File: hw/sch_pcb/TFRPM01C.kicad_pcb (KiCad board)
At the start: 2 copper layers, 37.5 x 19 mm, 23 parts, among them J1 HEADER_1x03, J2 SM04B-GHS-TB, J3 SM04B-GHS-TB, M2 M3, U1 PCF8583, U2 74HC1G14GW, U3 MIC5504-3.3YM5

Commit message: Edit
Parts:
- moved R1 0.44 mm to (141.5, 126.7)
- moved R2 0.44 mm to (137.2, 126.7)
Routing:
- net Net-(JP2-Pad2): track 9.91 -> 10.5 mm
- net GND: vias 61 -> 60
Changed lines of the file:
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@@
   )
   (footprint "Mlab_R:SMD-0805" (layer "B.Cu")
-    (at 141.478 126.3015 -90)
+    (at 141.478 126.746 -90)
     (property "Sheetfile" "TFRPM01C.kicad_sch")
     (property "Sheetname" "")
@@
   )
   (footprint "Mlab_R:SMD-0805" (layer "B.Cu")
-    (at 137.16 126.3015 90)
+    (at 137.16 126.746 90)
     (property "Sheetfile" "TFRPM01C.kicad_sch")
     (property "Sheetname" "")
@@
     (property "Sheetname" "")
     (attr exclude_from_pos_files)
-    (fp_text reference "JP2" (at 0 2.032) (layer "B.SilkS")
+    (fp_text reference "JP2" (at 1.016 -2.286) (layer "B.SilkS")
       (effects (font (size 1.3 1.3) (thickness 0.3)) (justify mirror))
     )
@@
   (via (at 138.176 136.903096) (size 0.8) (drill 0.4) (layers "F.Cu" "B.Cu") (net 1))
   (via (at 139.192 128.016) (size 0.8) (drill 0.4) (layers "F.Cu" "B.Cu") (net 1))
-  (via (at 136.906 128.524) (size 0.8) (drill 0.4) (layers "F.Cu" "B.Cu") (net 1))
   (via (at 143.002 135.382) (size 0.8) (drill 0.4) (layers "F.Cu" "B.Cu") (net 1))
   (via (at 143.764 138.684) (size 0.8) (drill 0.4) (layers "F.Cu" "B.Cu") (net 1))
@@
   (segment (start 129.032 140.462) (end 130.109096 140.462) (width 0.4) (layer "B.Cu") (net 2))
   (segment (start 130.109096 140.462) (end 130.874 139.697096) (width 0.4) (layer "B.Cu") (net 2))
-  (segment (start 141.478 127.254) (end 141.476548 127.255452) (width 0.5) (layer "B.Cu") (net 3))
+  (segment (start 141.478 131.696096) (end 141.478 127.6985) (width 0.5) (layer "B.Cu") (net 3))
   (segment (start 139.7 136.398) (end 138.303 135.001) (width 0.4) (layer "B.Cu") (net 3))
-  (segment (start 141.476548 131.697548) (end 138.303 134.871096) (width 0.5) (layer "B.Cu") (net 3))
+  (segment (start 138.303 134.871096) (end 141.478 131.696096) (width 0.5) (layer "B.Cu") (net 3))
   (segment (start 138.303 135.001) (end 138.303 134.871096) (width 0.4) (layer "B.Cu") (net 3))
   (segment (start 139.7 136.398) (end 139.7 138.242) (width 0.4) (layer "B.Cu") (net 3))
   (segment (start 138.303 134.871096) (end 138.43 134.871096) (width 0.5) (layer "B.Cu") (net 3))
-  (segment (start 141.476548 127.255452) (end 141.476548 131.697548) (width 0.5) (layer "B.Cu") (net 3))
   (segment (start 129.286 136.906) (end 131.094 136.906) (width 0.5) (layer "F.Cu") (net 4))
   (segment (start 133.604 136.906) (end 134.62 136.906) (width 0.5) (layer "F.Cu") (net 4))
@@
   (segment (start 133.769989 124.294011) (end 133.604 124.46) (width 0.5) (layer "B.Cu") (net 10))
   (segment (start 133.604 124.46) (end 133.604 125.984) (width 0.5) (layer "B.Cu") (net 10))
-  (segment (start 137.16 125.349) (end 136.105011 124.294011) (width 0.5) (layer "B.Cu") (net 10))
-  (segment (start 136.105011 124.294011) (end 133.769989 124.294011) (width 0.5) (layer "B.Cu") (net 10))
-  (segment (start 137.165511 125.354511) (end 141.472489 125.354511) (width 0.5) (layer "B.Cu") (net 10))
-  (segment (start 137.16 125.349) (end 137.165511 125.354511) (width 0.5) (layer "B.Cu") (net 10))
-  (segment (start 141.472489 125.354511) (end 141.478 125.349) (width 0.5) (layer "B.Cu") (net 10))
-  (segment (start 138.303 127.254) (end 139.192 126.365) (width 0.5) (layer "B.Cu") (net 11))
-  (segment (start 137.16 127.254) (end 138.303 127.254) (width 0.5) (layer "B.Cu") (net 11))
+  (segment (start 141.039011 125.354511) (end 141.478 125.7935) (width 0.5) (layer "B.Cu") (net 10))
+  (segment (start 137.598989 125.354511) (end 141.039011 125.354511) (width 0.5) (layer "B.Cu") (net 10))
+  (segment (start 135.660511 124.294011) (end 137.16 125.7935) (width 0.5) (layer "B.Cu") (net 10))
+  (segment (start 133.769989 124.294011) (end 135.660511 124.294011) (width 0.5) (layer "B.Cu") (net 10))
+  (segment (start 137.16 125.7935) (end 137.598989 125.354511) (width 0.5) (layer "B.Cu") (net 10))
+  (segment (start 140.329489 127.502489) (end 139.192 126.365) (width 0.5) (layer "B.Cu") (net 11))
+  (segment (start 138.557 126.365) (end 139.192 126.365) (width 0.5) (layer "B.Cu") (net 11))
+  (segment (start 137.2235 127.6985) (end 138.557 126.365) (width 0.5) (layer "B.Cu") (net 11))
+  (segment (start 137.16 127.6985) (end 137.2235 127.6985) (width 0.5) (layer "B.Cu") (net 11))
   (segment (start 138.303 132.331096) (end 140.329489 130.304607) (width 0.5) (layer "B.Cu") (net 11))
   (segment (start 140.329489 130.304607) (end 140.329489 127.502489) (width 0.5) (layer "B.Cu") (net 11))
-  (segment (start 139.192 126.365) (end 140.329489 127.502489) (width 0.5) (layer "B.Cu") (net 11))
   (zone (net 1) (net_name "GND") (layer "F.Cu") (hatch edge 0.508)
     (connect_pads thru_hole_only (clearance 0.2))

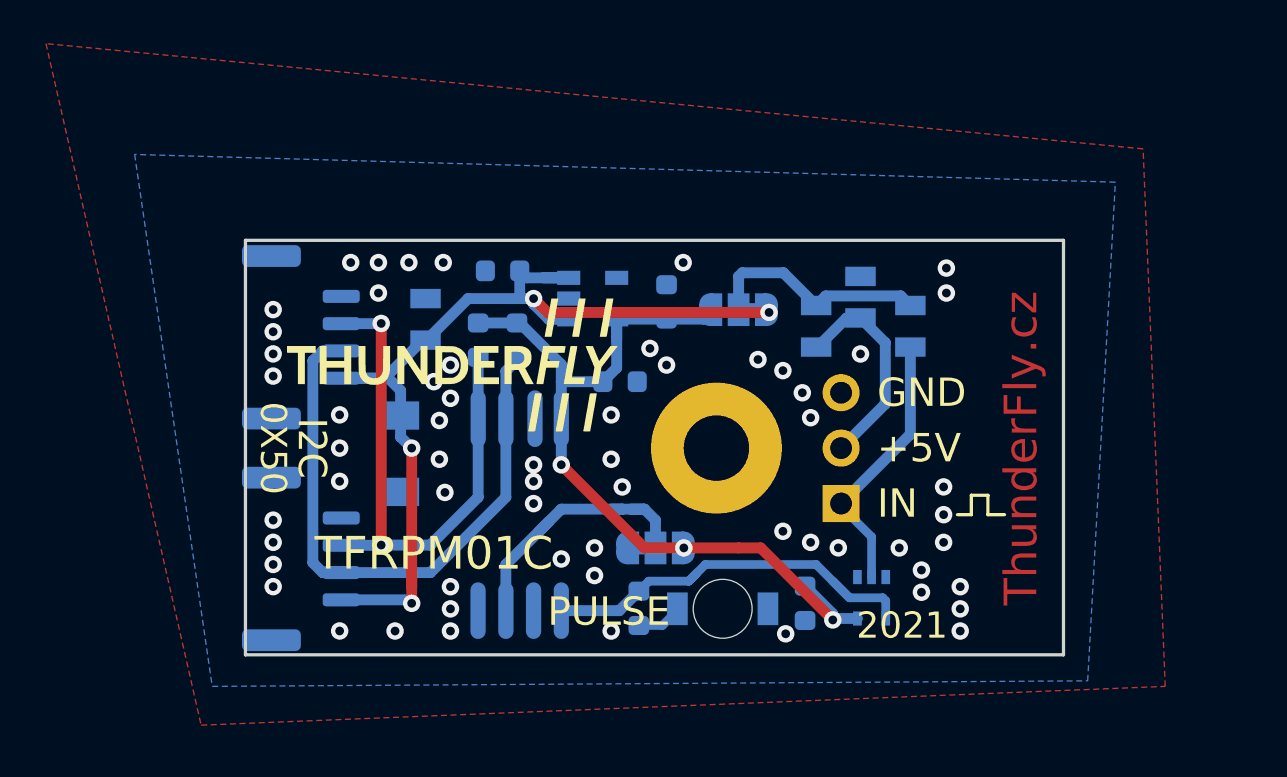
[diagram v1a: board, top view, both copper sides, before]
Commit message: update to newest kicad version, set schematic tempate, clean dps
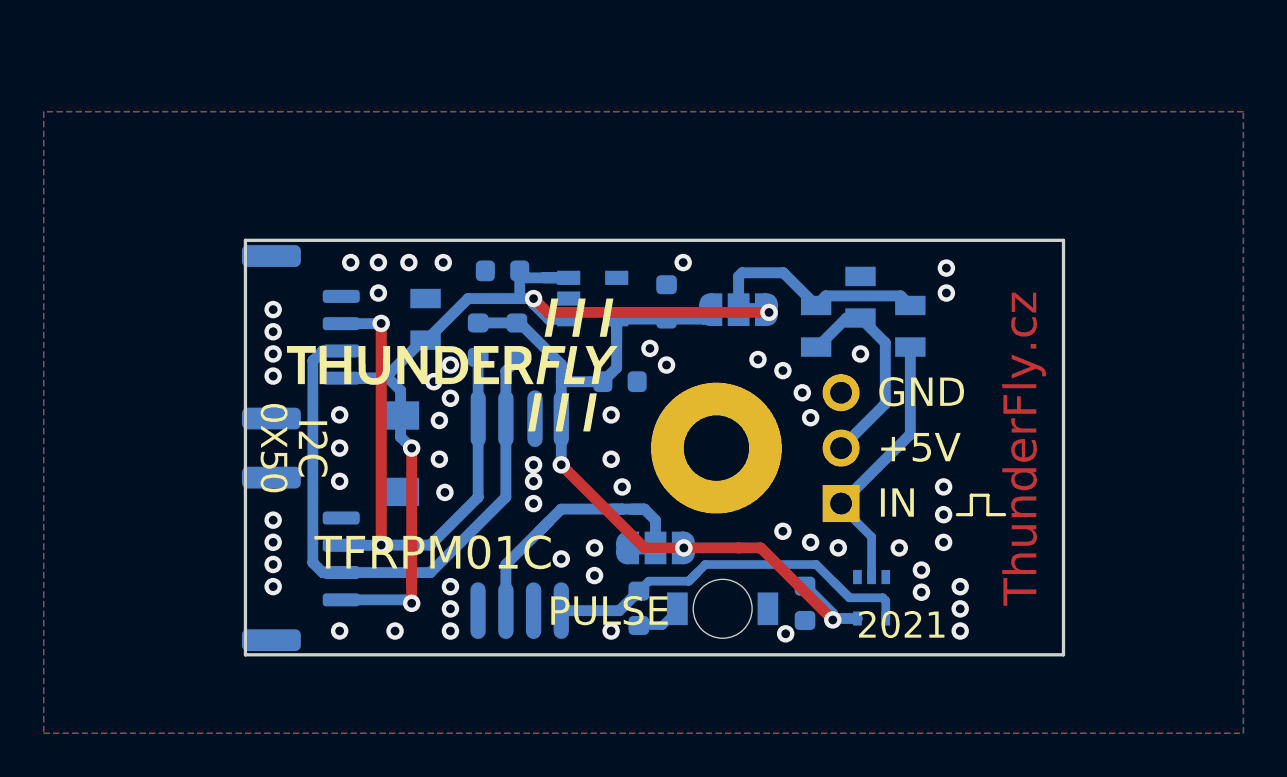
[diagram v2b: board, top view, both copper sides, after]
